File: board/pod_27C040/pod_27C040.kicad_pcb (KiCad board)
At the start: 2 copper layers, 39.4 x 57.2 mm, 13 parts, among them J1 EXT_D, J2 EXT_ADDR, J3 VCC_Probe, J4 GND_Probe, J5 ROM Lines, U1 74HCT02

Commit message: Added pod for 27C400, modified other pods
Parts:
- moved J5 38.2 mm to (162.6, 39.4), turned to 0 degrees
- moved R2 9.16 mm to (160.0, 90.2), turned to 0 degrees
- moved R1 5.68 mm to (160.0, 87.6), turned to 0 degrees
- moved D1 1.27 mm to (154.9, 90.2)
- renumbered J4 to GND, J3 to Vcc
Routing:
- net /A11: track 30.8 -> 80.5 mm
- net /A13: track 34.8 -> 80.9 mm, vias 0 -> 1
- net /A18: track 44.8 -> 85.6 mm
- net /A14: track 38.9 -> 78.7 mm, vias 0 -> 3
- net /A16: track 38.4 -> 76.6 mm
- net /A12: track 101.2 -> 67.0 mm, vias 0 -> 2
- net /D5: track 19.4 -> 47.9 mm, vias 0 -> 1
- net /A8: track 42.6 -> 69.7 mm, vias 1 -> 0
- net /EXT_VCC: track 41.8 -> 68.4 mm, vias 0 -> 3
- net /D4: track 19.5 -> 40.2 mm
- net /A2: track 35.6 -> 55.9 mm, vias 1 -> 3
- net /D6: track 19.4 -> 39.4 mm, vias 0 -> 3
- net /A7: track 35.6 -> 53.0 mm
- net /D0: track 24.2 -> 40.6 mm
- net /~SAFE_CE: track 17.9 -> 33.5 mm
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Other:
- board text added: "Vcc"
- board text removed: "Ext VCC"

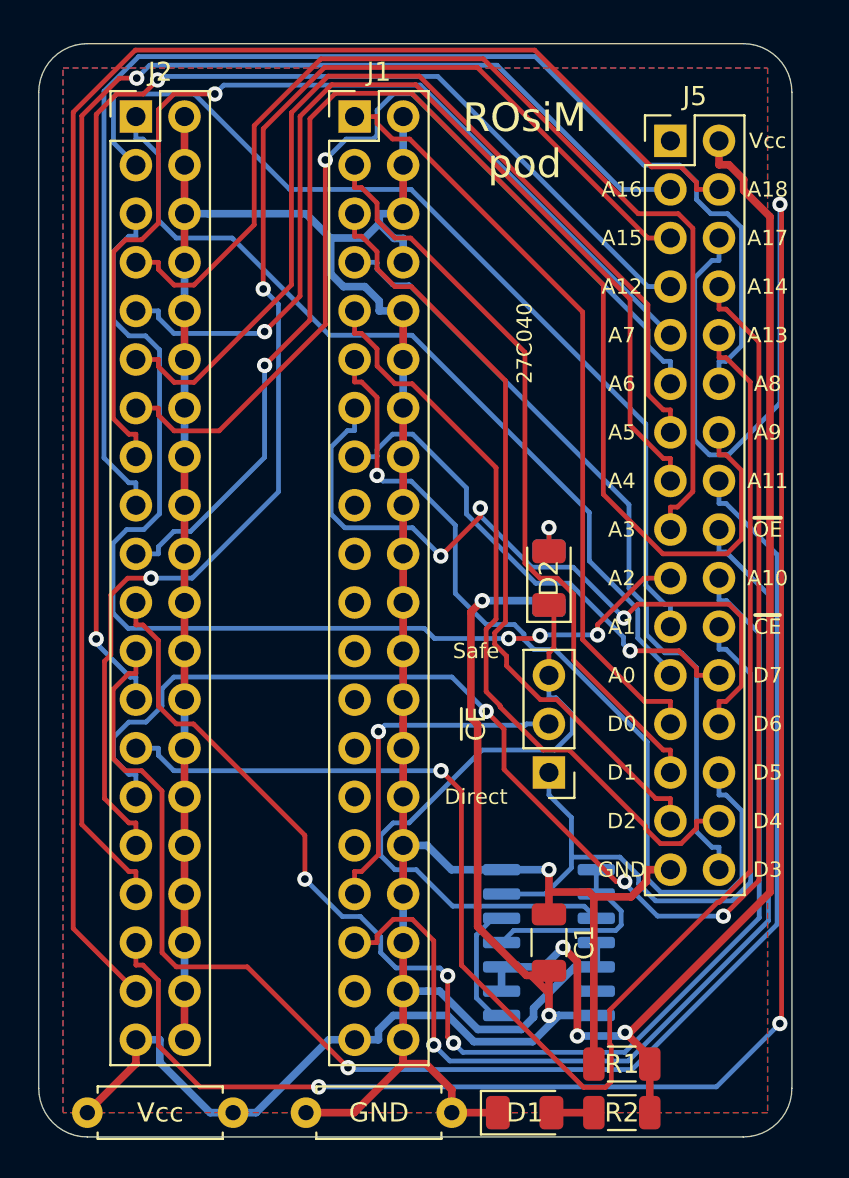
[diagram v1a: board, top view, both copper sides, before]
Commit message: Update all the pods to include the diode
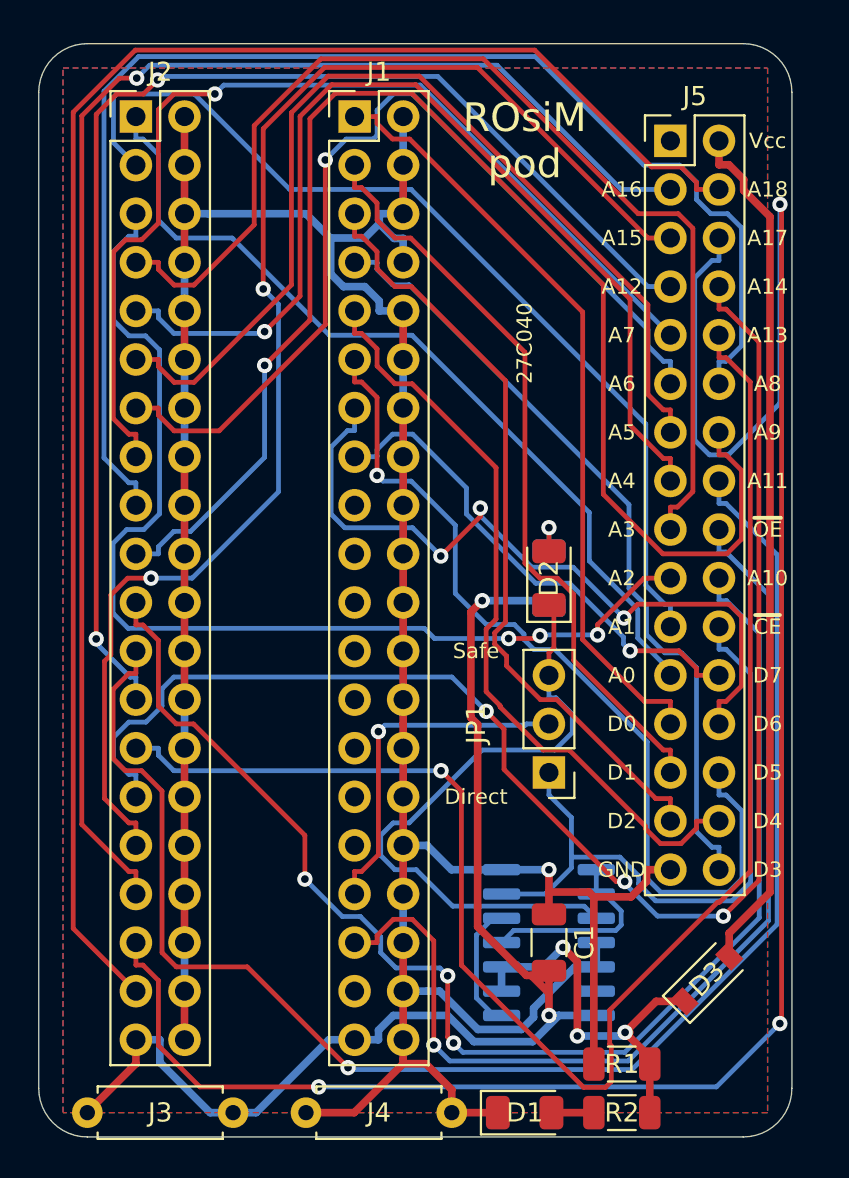
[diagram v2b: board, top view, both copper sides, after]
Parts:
- added D3: BAT48ZFILM, Diode_SMD:D_SOD-123, F.Cu at (164.5, 83.2)
- renumbered Vcc to J3, GND to J4, ~CE to JP1
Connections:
- J5 pad 2: /EXT_VCC -> Net-(D3-Pad2)
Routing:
- net /EXT_VCC: track 68.4 -> 21.2 mm
- net Net-(D3-Pad2): track 0.00 -> 44.9 mm

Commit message: Update 27C040 pod
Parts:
- removed D1: RED, LED_SMD:LED_1206_3216Metric
- removed R2: 1k, Resistor_SMD:R_1206_3216Metric
- added F1: 200mA, Fuse:Fuse_1206_3216Metric, F.Cu at (165.1, 87.6)
- moved D3 2.62 mm to (167.0, 82.5), turned to 90 degrees
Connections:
- D3 pad 1: /EXT_VCC -> Net-(D3-Pad1)
- R1 pad 2: /EXT_VCC -> VCC
- U1 pad 2: /EXT_VCC -> VCC
- U1 pad 3: /EXT_VCC -> VCC
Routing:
- net /EXT_VCC: track 21.2 -> 0.00 mm, vias 3 -> 0
- net VCC: track 63.8 -> 82.4 mm, vias 2 -> 5
- net Net-(D3-Pad1): track 0.00 -> 3.64 mm
- net GND: track 168.4 -> 166.0 mm
- net Net-(D1-Pad2): track 2.22 -> 0.00 mm
- net Net-(D3-Pad2): track 44.9 -> 43.3 mm
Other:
- board text added: "rev 1.1"
